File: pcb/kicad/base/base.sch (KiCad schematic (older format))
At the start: 43 parts, among them P1 J-Link SWD, P10 CONN_01X02, P11 CONN_01X02, P12 CONN_01X02, P2 SMA, P3 CONN_01X02, P4 USB Micro B, P5 Button, P6 Button, P7 Button, P8 Button, P9 Button, U1 SAMB11G18A-edit, Y1 32.768kHz, Y2 26MHz

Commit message: Add ground stitch vias and silk identifiers
Base station layout is finished, and artwork has been generated.
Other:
- note added: "April 7, 2017"
- note added: "LP_GPIO_3, 4, 5, 22, and 23 should be\nconfigured with internal pull-up resistors.\nAll other GPIOs should be configured\nwith internal pull-down resistors."
- note removed: "LP_GPIO_3, 4, 5, 22, and 23 should be configured\nwith internal pull-up resistors., while all other GPIOs\nshould be configured with internal pull-down resistors."
- note removed: "March 28, 2017"
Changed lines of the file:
@@
 Text Notes 7350 7500 0    60   ~ 0
 Base - Central
-Text Notes 8150 7650 0    60   ~ 0
-March 28, 2017
+Text Notes 8125 7650 0    60   ~ 0
+April 7, 2017
 Text Notes 10600 7650 0    60   ~ 0
 0.2
@@
 	1    0    0    -1
 $EndComp
-Text Notes 6650 1900 0    60   ~ 0
-LP_GPIO_3, 4, 5, 22, and 23 should be configured\nwith internal pull-up resistors., while all other GPIOs\nshould be configured with internal pull-down resistors.
 $Comp
 L CONN_01X02 P11
@@
 	1    0    0    -1
 $EndComp
+Text Notes 6650 1900 0    60   ~ 0
+LP_GPIO_3, 4, 5, 22, and 23 should be\nconfigured with internal pull-up resistors.\nAll other GPIOs should be configured\nwith internal pull-down resistors.
 $EndSCHEMATC

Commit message: Update pad sizes on pin headers and XBee
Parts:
- P1: footprint Misc:Socket_Strip_Straight_2x10_Pitch2.54mm_Drill0.64mm -> Misc:Socket_Strip_Straight_2x10_Pitch2.54mm_Drill0.762mm
- P10, P11, P12, P3, P5, P6, P7, P8, P9: footprint Misc:Socket_Strip_Straight_1x02_Pitch2.54mm_Drill0.64mm -> Misc:Socket_Strip_Straight_1x02_Pitch2.54mm_Drill0.762mm
- U1: footprint QFN-48-1EP_6x6mm_Pitch0.4mm -> Housings:QFN-48-1EP_6x6mm_Pitch0.4mm
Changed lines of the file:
@@
 F 0 "P1" H 7925 5800 50  0000 C CNN
 F 1 "J-Link SWD" V 7925 5250 50  0000 C CNN
-F 2 "Misc:Socket_Strip_Straight_2x10_Pitch2.54mm_Drill0.64mm" H 7925 4050 50  0001 C CNN
+F 2 "Misc:Socket_Strip_Straight_2x10_Pitch2.54mm_Drill0.762mm" H 7925 4050 50  0001 C CNN
 F 3 "" H 7925 4050 50  0000 C CNN
 	1    7925 5250
@@
 F 0 "P3" H 5500 1250 50  0000 C CNN
 F 1 "CONN_01X02" V 5600 1100 50  0000 C CNN
-F 2 "Misc:Socket_Strip_Straight_1x02_Pitch2.54mm_Drill0.64mm" H 5500 1100 50  0001 C CNN
+F 2 "Misc:Socket_Strip_Straight_1x02_Pitch2.54mm_Drill0.762mm" H 5500 1100 50  0001 C CNN
 F 3 "" H 5500 1100 50  0000 C CNN
 	1    5500 1100
@@
 F 0 "P5" H 8950 4200 50  0000 C CNN
 F 1 "Button" H 8950 4000 50  0000 C CNN
-F 2 "Misc:Socket_Strip_Straight_1x02_Pitch2.54mm_Drill0.64mm" H 8950 2900 50  0001 C CNN
+F 2 "Misc:Socket_Strip_Straight_1x02_Pitch2.54mm_Drill0.762mm" H 8950 2900 50  0001 C CNN
 F 3 "" H 8950 2900 50  0000 C CNN
 	1    8950 4100
@@
 F 0 "U1" H 5850 3500 50  0000 C CNN
 F 1 "SAMB11G18A-edit" H 6400 2450 50  0000 C CNN
-F 2 "QFN-48-1EP_6x6mm_Pitch0.4mm" H 6800 2375 50  0001 C CIN
+F 2 "Housings:QFN-48-1EP_6x6mm_Pitch0.4mm" H 6800 2375 50  0001 C CIN
 F 3 "" H 5850 3500 50  0000 C CNN
 	1    5850 3500
@@
 F 0 "P7" H 8950 4750 50  0000 C CNN
 F 1 "Button" H 8950 4550 50  0000 C CNN
-F 2 "Misc:Socket_Strip_Straight_1x02_Pitch2.54mm_Drill0.64mm" H 8950 3450 50  0001 C CNN
+F 2 "Misc:Socket_Strip_Straight_1x02_Pitch2.54mm_Drill0.762mm" H 8950 3450 50  0001 C CNN
 F 3 "" H 8950 3450 50  0000 C CNN
 	1    8950 4650
@@
 F 0 "P6" H 8950 4475 50  0000 C CNN
 F 1 "Button" H 8950 4275 50  0000 C CNN
-F 2 "Misc:Socket_Strip_Straight_1x02_Pitch2.54mm_Drill0.64mm" H 8950 3175 50  0001 C CNN
+F 2 "Misc:Socket_Strip_Straight_1x02_Pitch2.54mm_Drill0.762mm" H 8950 3175 50  0001 C CNN
 F 3 "" H 8950 3175 50  0000 C CNN
 	1    8950 4375
@@
 F 0 "P8" H 8950 5025 50  0000 C CNN
 F 1 "Button" H 8950 4825 50  0000 C CNN
-F 2 "Misc:Socket_Strip_Straight_1x02_Pitch2.54mm_Drill0.64mm" H 8950 3725 50  0001 C CNN
+F 2 "Misc:Socket_Strip_Straight_1x02_Pitch2.54mm_Drill0.762mm" H 8950 3725 50  0001 C CNN
 F 3 "" H 8950 3725 50  0000 C CNN
 	1    8950 4925
@@
 F 0 "P9" H 8950 5300 50  0000 C CNN
 F 1 "Button" H 8950 5100 50  0000 C CNN
-F 2 "Misc:Socket_Strip_Straight_1x02_Pitch2.54mm_Drill0.64mm" H 8950 4000 50  0001 C CNN
+F 2 "Misc:Socket_Strip_Straight_1x02_Pitch2.54mm_Drill0.762mm" H 8950 4000 50  0001 C CNN
 F 3 "" H 8950 4000 50  0000 C CNN
 	1    8950 5200
@@
 F 0 "P10" H 8950 3875 50  0000 C CNN
 F 1 "CONN_01X02" V 9050 3725 50  0000 C CNN
-F 2 "Misc:Socket_Strip_Straight_1x02_Pitch2.54mm_Drill0.64mm" H 8950 3725 50  0001 C CNN
+F 2 "Misc:Socket_Strip_Straight_1x02_Pitch2.54mm_Drill0.762mm" H 8950 3725 50  0001 C CNN
 F 3 "" H 8950 3725 50  0000 C CNN
 	1    8950 3725
@@
 F 0 "P11" H 4850 1250 50  0000 C CNN
 F 1 "CONN_01X02" V 4950 1100 50  0000 C CNN
-F 2 "Misc:Socket_Strip_Straight_1x02_Pitch2.54mm_Drill0.64mm" H 4850 1100 50  0001 C CNN
+F 2 "Misc:Socket_Strip_Straight_1x02_Pitch2.54mm_Drill0.762mm" H 4850 1100 50  0001 C CNN
 F 3 "" H 4850 1100 50  0000 C CNN
 	1    4850 1100
@@
 F 0 "P12" H 4150 1250 50  0000 C CNN
 F 1 "CONN_01X02" V 4250 1100 50  0000 C CNN
-F 2 "Misc:Socket_Strip_Straight_1x02_Pitch2.54mm_Drill0.64mm" H 4150 1100 50  0001 C CNN
+F 2 "Misc:Socket_Strip_Straight_1x02_Pitch2.54mm_Drill0.762mm" H 4150 1100 50  0001 C CNN
 F 3 "" H 4150 1100 50  0000 C CNN
 	1    4150 1100

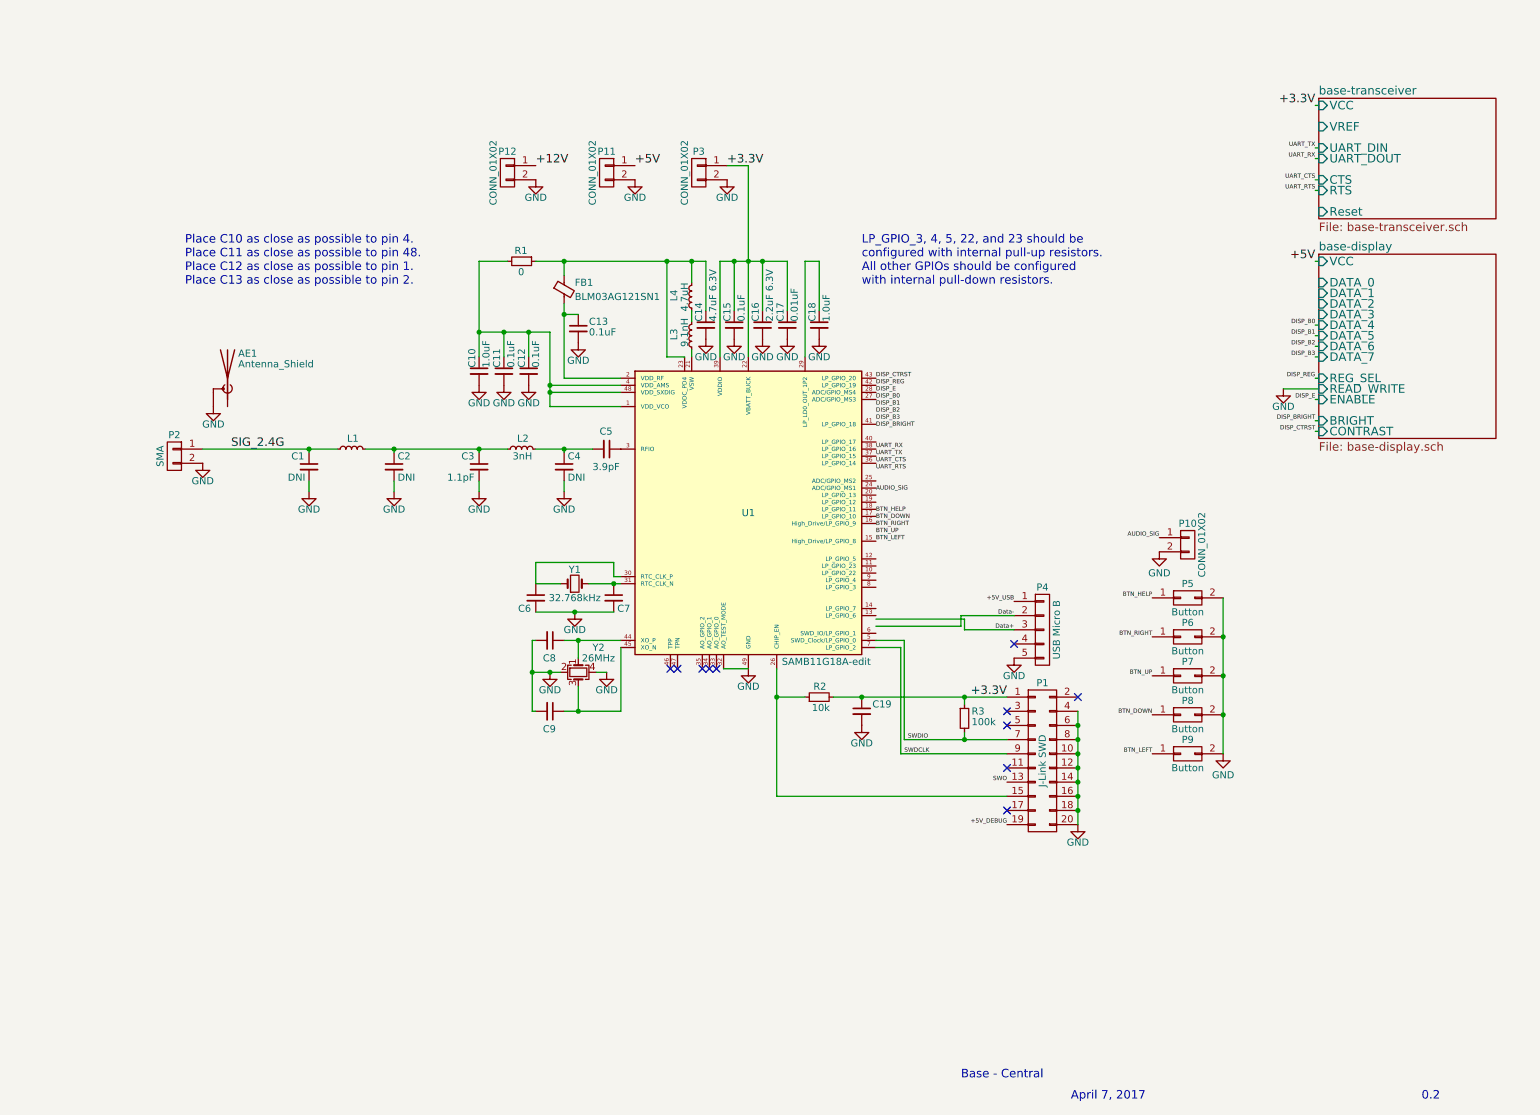
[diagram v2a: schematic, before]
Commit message: Revamp base station layout
26MHz crystal moved to the top layer after reducing pad size. Slight
spacing with SMD components to avoid difficulties with hand soldering.
Component sections moved around for a more compact final layout. Antenna
section still needs to changed depending on transmission line matching
circuit. Traces to be finished.
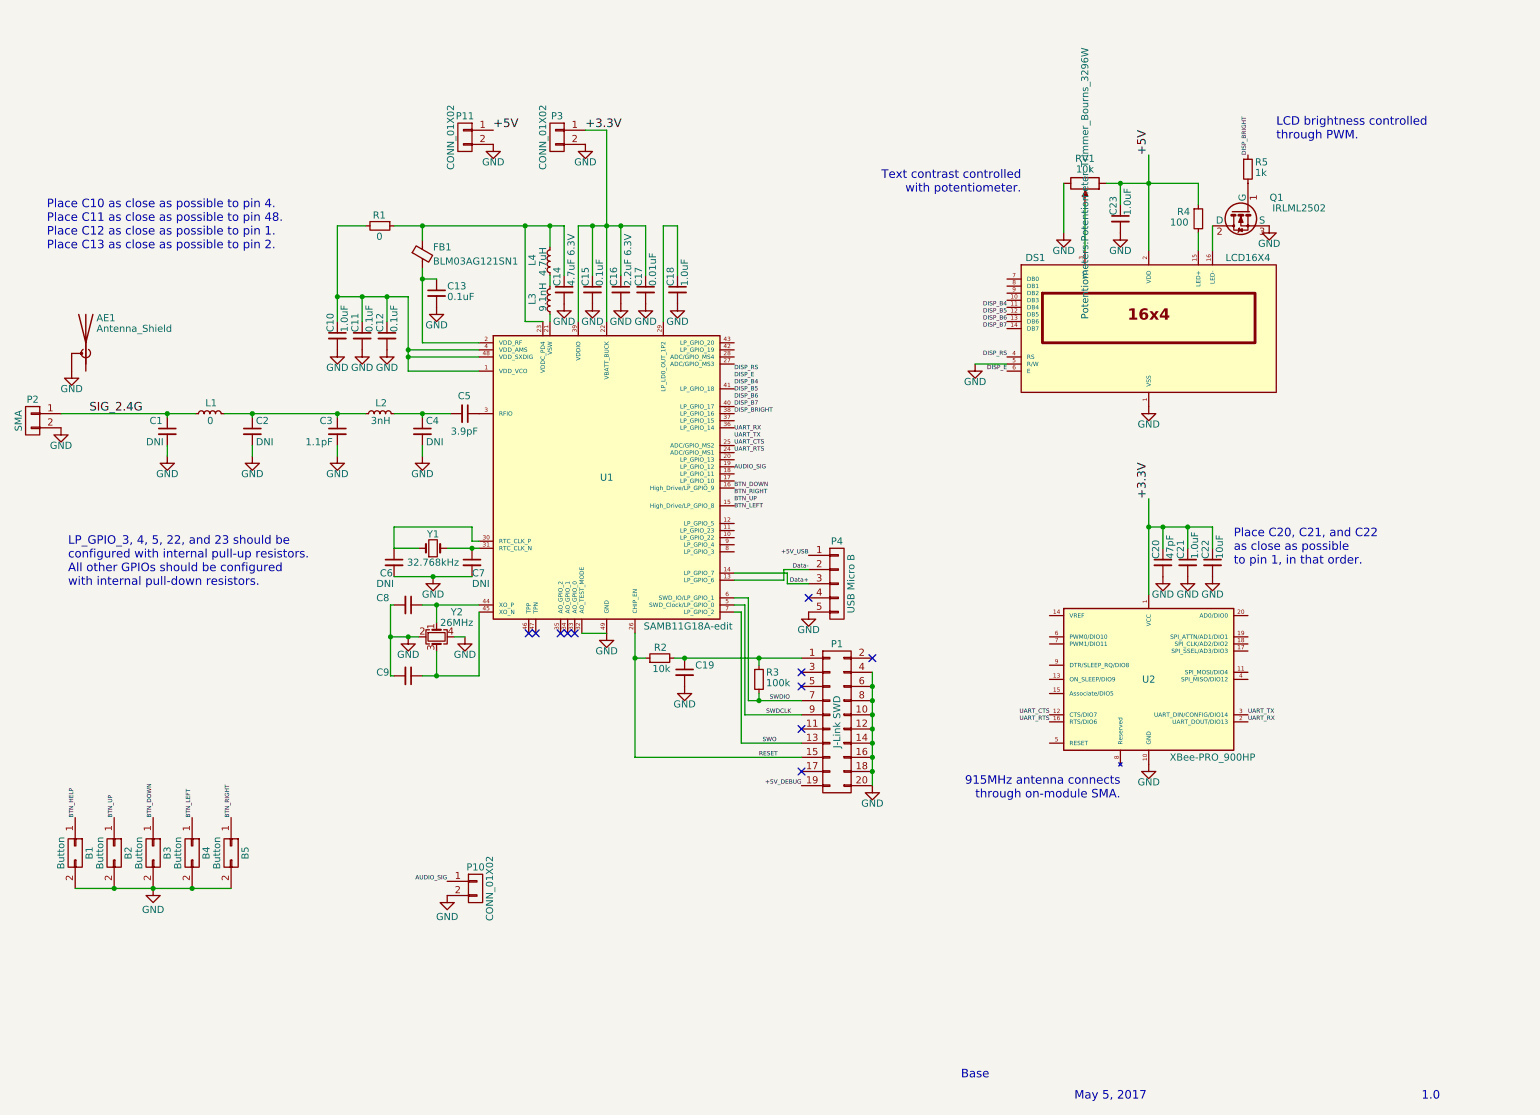
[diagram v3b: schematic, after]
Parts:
- removed P12: CONN_01X02, Misc:Socket_Strip_Straight_1x02_Pitch2.54mm_Drill0.762mm, symbol CONN_01X02
- added C20: 47pF, Capacitors_SMD:C_0402, symbol C_Small
- added C21, C23: 1.0uF, Capacitors_SMD:C_0402, symbol C_Small
- added C22: 10uF, Capacitors_SMD:C_0402, symbol C_Small
- added DS1: LCD16X4, CFAH1604A, symbol LCD16X4
- added Q1: IRLML2502, TO_SOT_Packages_SMD:SOT-23, symbol IRLB8721PBF
- added R4: 100, Capacitors_SMD:C_0402, symbol R_Small
- added R5: 1k, Capacitors_SMD:C_0402, symbol R_Small
- added RV1: 10k, Potentiometers:Potentiometer_Trimmer_Bourns_3296W, symbol POT
- added U2: XBee-PRO_900HP, Digi_XBee-PRO_TH, symbol XBee-PRO_900HP
- B1: renamed from P5; footprint Misc:Socket_Strip_Straight_1x02_Pitch2.54mm_Drill0.762mm -> Misc:E-Switch_KS01Q01
- B2: renamed from P6; footprint Misc:Socket_Strip_Straight_1x02_Pitch2.54mm_Drill0.762mm -> Misc:E-Switch_KS01Q01
- B3: renamed from P7; footprint Misc:Socket_Strip_Straight_1x02_Pitch2.54mm_Drill0.762mm -> Misc:E-Switch_KS01Q01
- B4: renamed from P8; footprint Misc:Socket_Strip_Straight_1x02_Pitch2.54mm_Drill0.762mm -> Misc:E-Switch_KS01Q01
- B5: renamed from P9; footprint Misc:Socket_Strip_Straight_1x02_Pitch2.54mm_Drill0.762mm -> Misc:E-Switch_KS01Q01
- C6, C7: value C_Small -> DNI
- L1: value L_Small -> 0
- Y2: footprint Crystals:Crystal_SMD_3225-4pin_3.2x2.5mm_HandSoldering -> Crystals:Crystal_SMD_2520-4pin_2.5x2.0mm
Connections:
- net +3.3V: now also C20.1, C21.1, C22.1, U2.1 (VCC); no longer C19.1, P1.1 (P1), R2.2, R3.1
- net +5V: now also C23.1, DS1.2 (VDD), R4.1, RV1.1
- net BTN_DOWN: now also B3.1 (P1), U1.16 (High_Drive/LP_GPIO_9); no longer B4.1 (P1)
- net BTN_LEFT: now also B4.1 (P1); no longer B5.1 (P1), U1.15 (High_Drive/LP_GPIO_8)
- net BTN_RIGHT: now also B5.1 (P1); no longer B2.1 (P1)
- net BTN_UP: now also B2.1 (P1); no longer B3.1 (P1)
- net DISP_BRIGHT: now also U1.38 (LP_GPIO_16), R5.1
- net DISP_E: now also DS1.6 (E); no longer U1.28 (ADC/GPIO_MS4)
- net Data+: now also U1.14 (LP_GPIO_7)
- net Data-: now also U1.13 (LP_GPIO_6)
- net GND: now also C20.2, C21.2, C22.2, C23.2, DS1.1 (VSS), DS1.5 (R/W), Q1.3 (S), RV1.3, U2.10 (GND)
- net SWDCLK: now also U1.5 (SWD_Clock/LP_GPIO_0); no longer U1.7 (LP_GPIO_2)
- net SWDIO: now also U1.6 (SWD_IO/LP_GPIO_1); no longer U1.5 (SWD_Clock/LP_GPIO_0)
- net SWO: now also U1.7 (LP_GPIO_2)
- net UART_CTS: now also U1.25 (ADC/GPIO_MS2), U2.12 (CTS/DIO7); no longer U1.36 (LP_GPIO_14)
- net UART_RTS: now also U1.24 (ADC/GPIO_MS1), U2.16 (RTS/DIO6)
- net UART_RX: now also U2.2 (UART_DOUT/DIO13); no longer U1.38 (LP_GPIO_16)
- net UART_TX: now also U2.3 (UART_DIN/CONFIG/DIO14); no longer U1.37 (LP_GPIO_15)
- net RESET: now reaches P1.15 (P15), R2.1, U1.26 (CHIP_EN)
- net DISP_B7: now reaches U1.40 (LP_GPIO_17)
- net DISP_B7: now also DS1.14 (DB7)
- net DISP_B0: no longer names the net of U1.27 (ADC/GPIO_MS3)
- net DISP_CTRST: no longer names the net of U1.43 (LP_GPIO_20)
- net DISP_REG: no longer names the net of U1.42 (LP_GPIO_19)
- new net: C19.1, P1.1 (P1), R2.2, R3.1
- new net: DS1.15 (LED+), R4.2
- new net: DS1.16 (LED-), Q1.2 (D)
- new net: DS1.3 (VO), RV1.2
- new net: Q1.1 (G), R5.2
- new net DISP_B4: DS1.11 (DB4)
- new net DISP_B5: DS1.12 (DB5)
- new net DISP_B6: DS1.13 (DB6)
- new net DISP_RS: DS1.4 (RS)
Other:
- note added: "1.0"
- note added: "915MHz antenna connects\nthrough on-module SMA."
- note added: "Base"
- note added: "LCD brightness controlled\nthrough PWM."
- note added: "May 5, 2017"
- note added: "Place C20, C21, and C22\nas close as possible\nto pin 1, in that order."
- note added: "Text contrast controlled\nwith potentiometer."
- note removed: "0.2"
- note removed: "April 7, 2017"
- note removed: "Base - Central"
- moved on the sheet: AE1, B1, B2, B3, B4, B5, C1, C10, C11, C12, C13, C14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

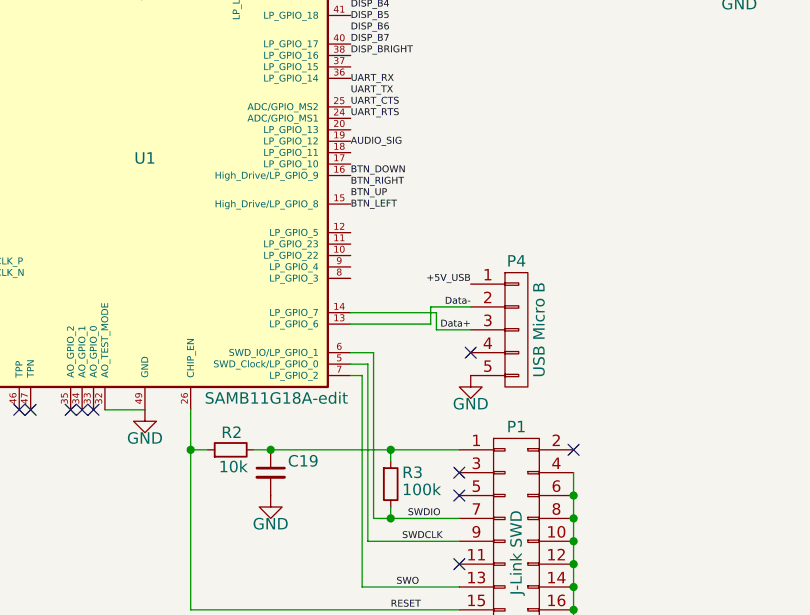
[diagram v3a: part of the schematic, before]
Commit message: Update base component placement and routing
New base station revision updated for a more complete prototype. Buttons
placed into layout, and SWD debugger pin header fixed.
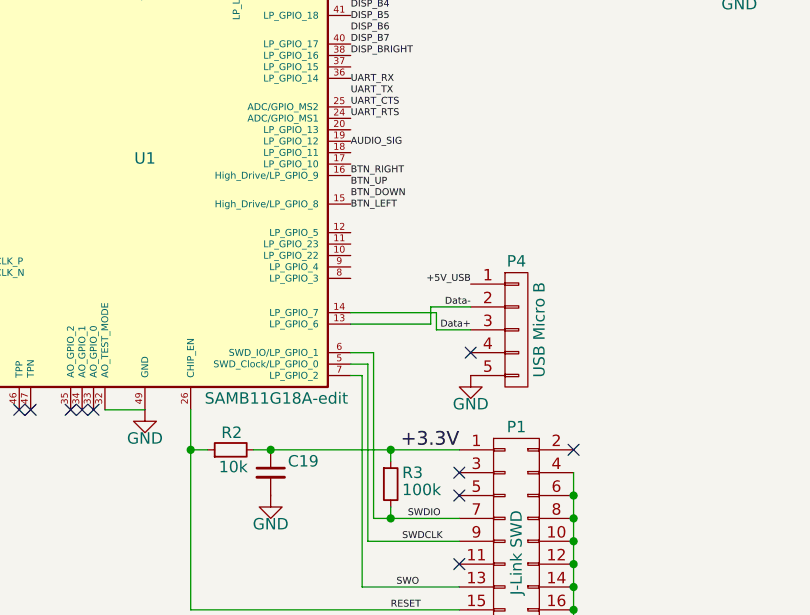
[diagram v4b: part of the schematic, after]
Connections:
- net +3.3V: now also C19.1, P1.1 (P1), R2.2, R3.1
- net BTN_DOWN: no longer U1.16 (High_Drive/LP_GPIO_9)
- net BTN_RIGHT: now also U1.16 (High_Drive/LP_GPIO_9)
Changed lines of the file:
@@
 Text Label 1925 5650 1    30   ~ 0
 BTN_LEFT
+Text Label 5750 3325 0    30   ~ 0
+BTN_RIGHT
 Text Label 5750 3375 0    30   ~ 0
-BTN_RIGHT
+BTN_UP
 Text Label 5750 3425 0    30   ~ 0
-BTN_UP
-Text Label 5750 3325 0    30   ~ 0
 BTN_DOWN
 Text Label 5750 3475 0    30   ~ 0
@@
 	1    0    0    -1
 $EndComp
+Text Label 6225 4525 2    60   ~ 0
++3.3V
 $EndSCHEMATC
